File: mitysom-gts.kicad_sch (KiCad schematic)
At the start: 9 parts, among them J1 Plug_Samtec_SEAM-50-02.0-L-08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

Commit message: [#100764] Swap DC-SCM PCIe P/N for better PCB layout
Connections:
- net DC_SCM_PCIE.TX0+: now also J1.G38 (GTSL1B_RX_CH0_N); no longer J1.G39 (GTSL1B_RX_CH0_P)
- net DC_SCM_PCIE.TX0-: now also J1.G39 (GTSL1B_RX_CH0_P); no longer J1.G38 (GTSL1B_RX_CH0_N)
- net DC_SCM_PCIE.TX1+: now also J1.A36 (GTSL1B_RX_CH1_N); no longer J1.A37 (GTSL1B_RX_CH1_P)
- net DC_SCM_PCIE.TX1-: now also J1.A37 (GTSL1B_RX_CH1_P); no longer J1.A36 (GTSL1B_RX_CH1_N)
- net DC_SCM_PCIE.TX2+: now also J1.G42 (GTSL1B_RX_CH2_N); no longer J1.G43 (GTSL1B_RX_CH2_P)
- net DC_SCM_PCIE.TX2-: now also J1.G43 (GTSL1B_RX_CH2_P); no longer J1.G42 (GTSL1B_RX_CH2_N)
- net DC_SCM_PCIE.TX3+: now also J1.A40 (GTSL1B_RX_CH3_N); no longer J1.A41 (GTSL1B_RX_CH3_P)
- net DC_SCM_PCIE.TX3-: now also J1.A41 (GTSL1B_RX_CH3_P); no longer J1.A40 (GTSL1B_RX_CH3_N)
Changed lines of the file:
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@@
 		)
 	)
-	(label "DC_SCM_PCIE.TX1+"
-		(at 133.4377 187.96 0)
+	(label "DC_SCM_PCIE.TX3+"
+		(at 133.35 200.66 0)
 		(effects
 			(font
@@
 		)
 	)
-	(label "DC_SCM_PCIE.TX3+"
-		(at 133.4377 198.12 0)
+	(label "DC_SCM_PCIE.TX1-"
+		(at 133.35 187.96 0)
 		(effects
 			(font
@@
 		)
 	)
-	(label "DC_SCM_PCIE.TX2-"
-		(at 133.35 195.58 0)
+	(label "DC_SCM_PCIE.TX3-"
+		(at 133.35 198.12 0)
 		(effects
 			(font
@@
 		)
 	)
-	(label "DC_SCM_PCIE.TX3-"
-		(at 133.4377 200.66 0)
+	(label "DC_SCM_PCIE.TX2-"
+		(at 133.35 193.04 0)
 		(effects
 			(font
@@
 		)
 	)
+	(label "DC_SCM_PCIE.TX0-"
+		(at 133.35 182.88 0)
+		(effects
+			(font
+				(size 1.27 1.27)
+			)
+			(justify left bottom)
+		)
+	)
 	(label "DP.TXD0-"
 		(at 280.67 119.38 0)
@@
 		)
 	)
+	(label "DC_SCM_PCIE.TX0+"
+		(at 133.35 185.42 0)
+		(effects
+			(font
+				(size 1.27 1.27)
+			)
+			(justify left bottom)
+		)
+	)
 	(label "ROOTPORT.TX0-"
 		(at 135.89 130.81 0)
@@
 		)
 	)
-	(label "DC_SCM_PCIE.TX0-"
-		(at 133.4377 185.42 0)
-		(effects
-			(font
-				(size 1.27 1.27)
-			)
-			(justify left bottom)
-		)
-	)
 	(label "PCIEx4_CLK.CLK+"
 		(at 134.62 204.47 0)
@@
 		)
 	)
-	(label "DC_SCM_PCIE.TX1-"
-		(at 133.4377 190.5 0)
-		(effects
-			(font
-				(size 1.27 1.27)
-			)
-			(justify left bottom)
-		)
-	)
 	(label "156_25MHz_CLK.+"
 		(at 133.35 154.94 0)
@@
 		)
 	)
+	(label "DC_SCM_PCIE.TX2+"
+		(at 133.35 195.58 0)
+		(effects
+			(font
+				(size 1.27 1.27)
+			)
+			(justify left bottom)
+		)
+	)
 	(label "DC_SCM_PCIE.RX2+"
 		(at 133.4377 171.45 0)
@@
 		)
 	)
-	(label "DC_SCM_PCIE.TX0+"
-		(at 133.4377 182.88 0)
+	(label "DC_SCM_PCIE.TX1+"
+		(at 133.35 190.5 0)
 		(effects
 			(font
@@
 		(effects
 			(font
-				(size 1.27 1.27)
-			)
-			(justify left bottom)
-		)
-	)
-	(label "DC_SCM_PCIE.TX2+"
-		(at 133.35 193.04 0)
-		(effects
-			(font

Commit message: [#100707] Place PCIe AC coupling capacitors
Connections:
- net DC_SCM_PCIE.RX1+: now also J1.H40 (GTSL1B_TX_CH1_N); no longer J1.H41 (GTSL1B_TX_CH1_P)
- net DC_SCM_PCIE.RX1-: now also J1.H41 (GTSL1B_TX_CH1_P); no longer J1.H40 (GTSL1B_TX_CH1_N)
- net DC_SCM_PCIE.RX3+: now also J1.H48 (GTSL1B_TX_CH3_N); no longer J1.H49 (GTSL1B_TX_CH3_P)
- net DC_SCM_PCIE.RX3-: now also J1.H49 (GTSL1B_TX_CH3_P); no longer J1.H48 (GTSL1B_TX_CH3_N)
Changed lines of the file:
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@@
 		)
 	)
-	(label "DC_SCM_PCIE.RX3+"
+	(label "DC_SCM_PCIE.RX3-"
 		(at 133.4377 176.53 0)
 		(effects
@@
 		)
 	)
-	(label "DC_SCM_PCIE.RX3-"
+	(label "DC_SCM_PCIE.RX3+"
 		(at 133.4377 179.07 0)
 		(effects
@@
 		)
 	)
-	(label "DC_SCM_PCIE.RX1-"
+	(label "DC_SCM_PCIE.RX1+"
 		(at 133.4076 168.91 0)
 		(effects
@@
 		)
 	)
-	(label "DC_SCM_PCIE.RX1+"
+	(label "DC_SCM_PCIE.RX1-"
 		(at 133.4076 166.37 0)
 		(effects

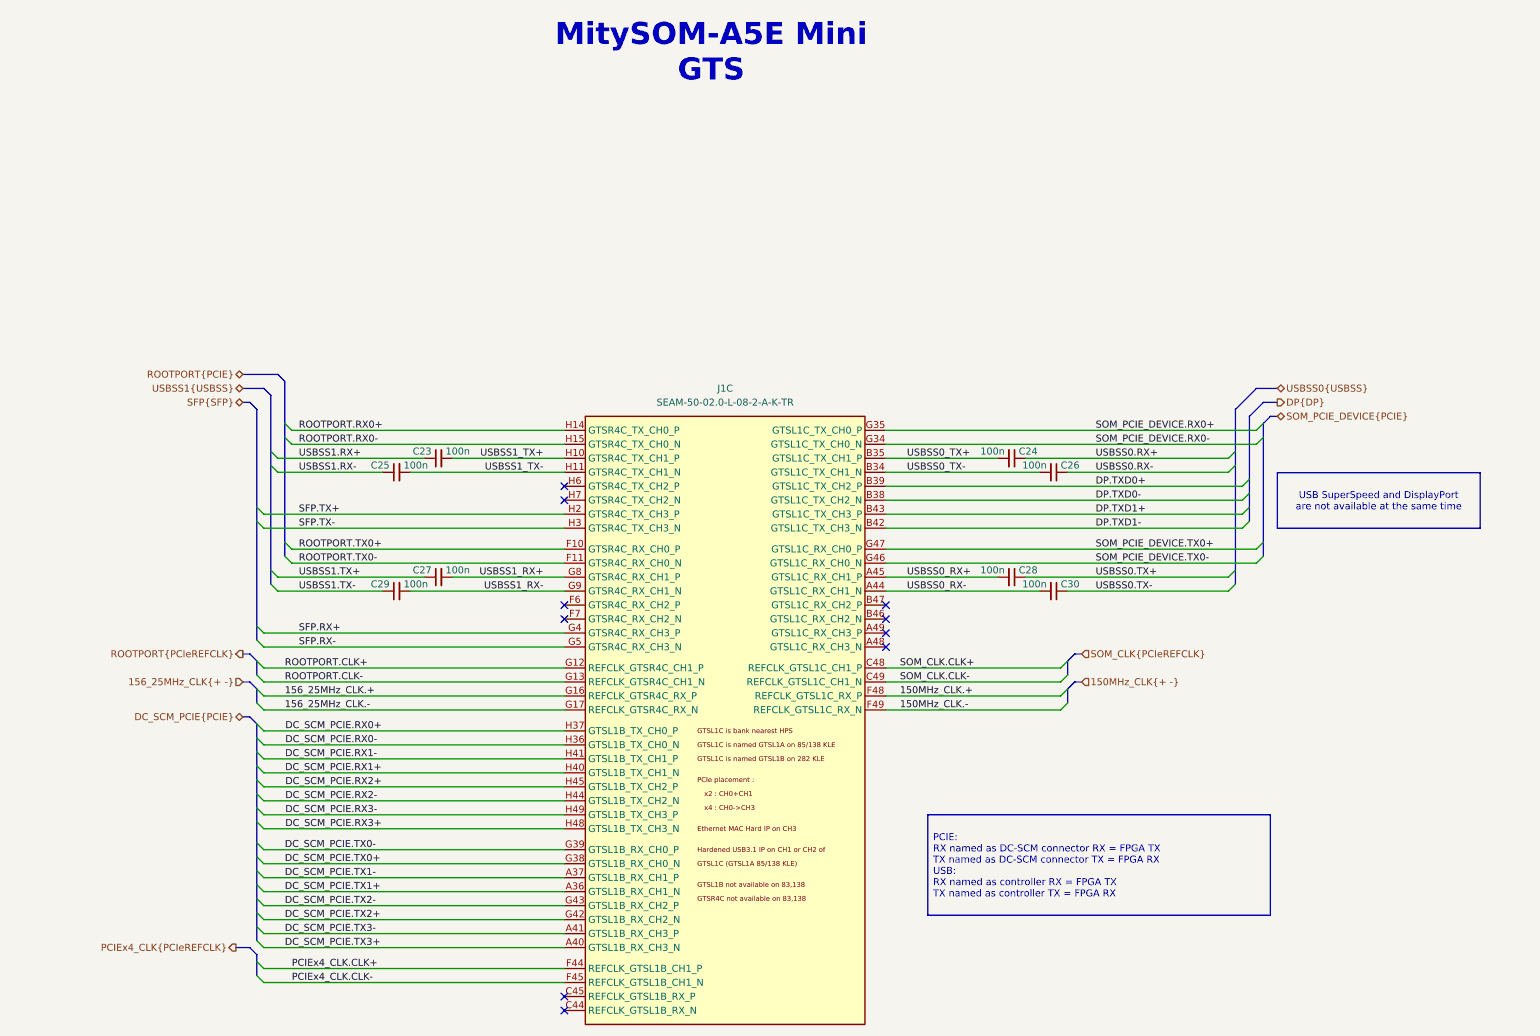
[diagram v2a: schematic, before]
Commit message: [#100707] Move PCIe AC coupling capacitrs on the schematic, close to TX source, add 0Rs to DC-SCM PCIe
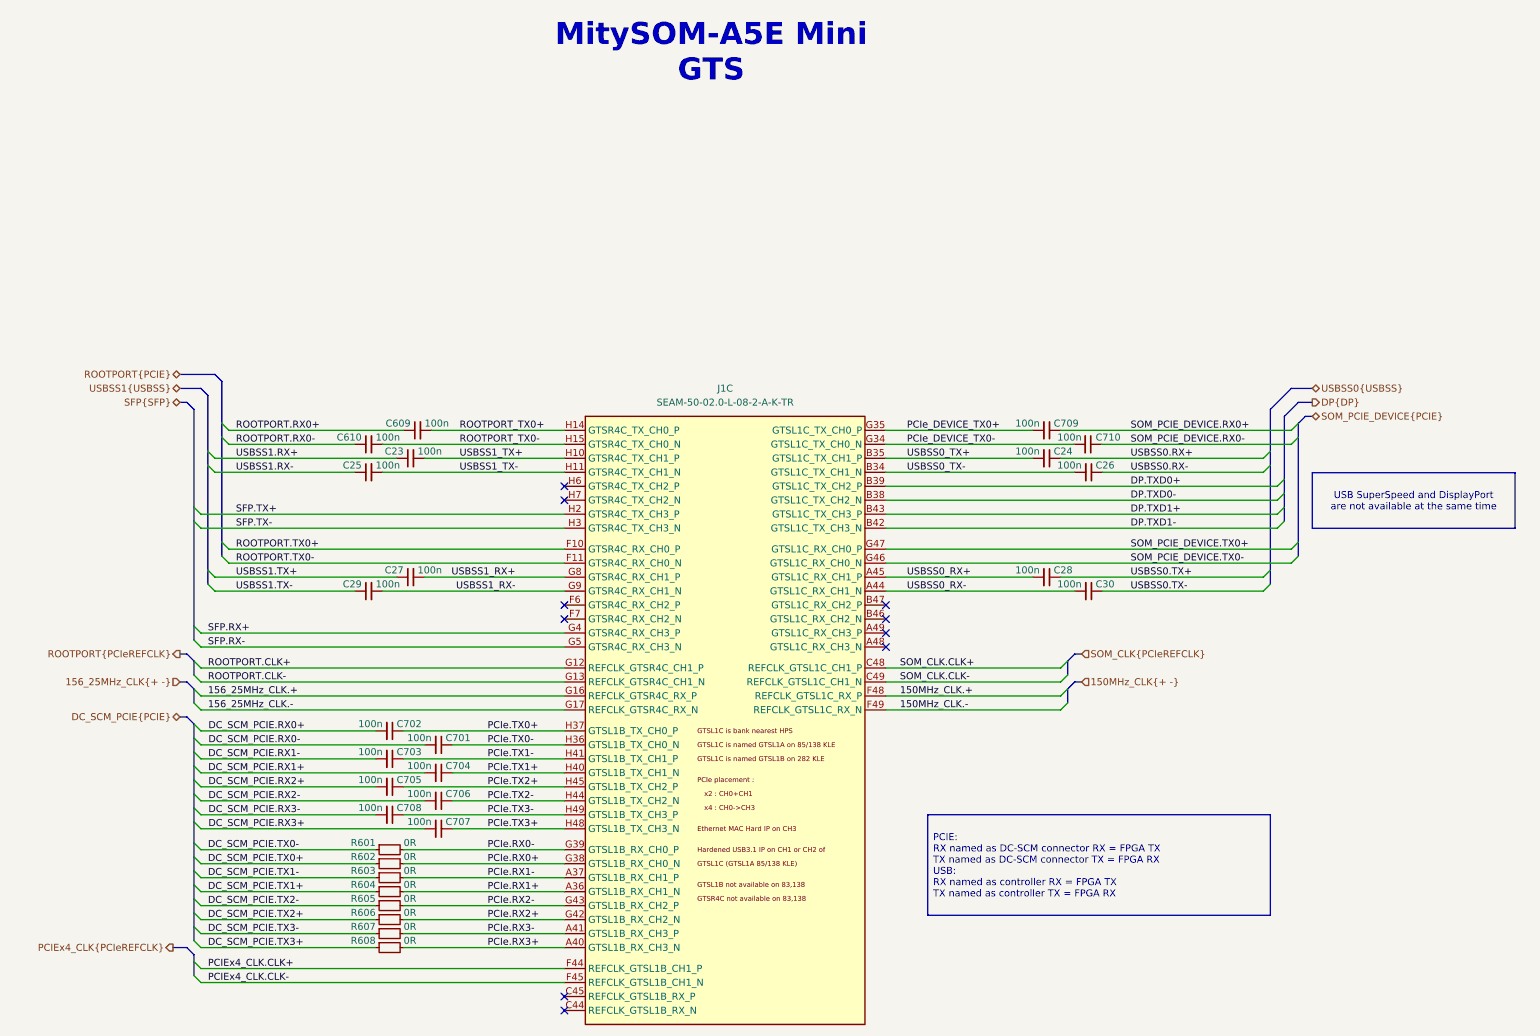
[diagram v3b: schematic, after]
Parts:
- added C609, C610, C701, C702, C703, C704, C705, C706, C707, C708, C709, C710: C_100n_0402, antmicro-footprints:C_0402_1005Metric, symbol antmicroCapacitors0402:C_100n_0402
- added R601, R602, R603, R604, R605, R606, R607, R608: R_0R_0402, antmicro-footprints:R_0402_1005Metric, symbol antmicroResistors0402:R_0R_0402
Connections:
- net DC_SCM_PCIE.RX0+: now also C702.2; no longer J1.H37 (GTSL1B_TX_CH0_P)
- net DC_SCM_PCIE.RX0-: now also C701.2; no longer J1.H36 (GTSL1B_TX_CH0_N)
- net DC_SCM_PCIE.RX1+: now also C704.2; no longer J1.H40 (GTSL1B_TX_CH1_N)
- net DC_SCM_PCIE.RX1-: now also C703.2; no longer J1.H41 (GTSL1B_TX_CH1_P)
- net DC_SCM_PCIE.RX2+: now also C705.2; no longer J1.H45 (GTSL1B_TX_CH2_P)
- net DC_SCM_PCIE.RX2-: now also C706.2; no longer J1.H44 (GTSL1B_TX_CH2_N)
- net DC_SCM_PCIE.RX3+: now also C707.2; no longer J1.H48 (GTSL1B_TX_CH3_N)
- net DC_SCM_PCIE.RX3-: now also C708.2; no longer J1.H49 (GTSL1B_TX_CH3_P)
- net DC_SCM_PCIE.TX0+: now also R602.1; no longer J1.G38 (GTSL1B_RX_CH0_N)
- net DC_SCM_PCIE.TX0-: now also R601.1; no longer J1.G39 (GTSL1B_RX_CH0_P)
- net DC_SCM_PCIE.TX1+: now also R604.1; no longer J1.A36 (GTSL1B_RX_CH1_N)
- net DC_SCM_PCIE.TX1-: now also R603.1; no longer J1.A37 (GTSL1B_RX_CH1_P)
- net DC_SCM_PCIE.TX2+: now also R606.1; no longer J1.G42 (GTSL1B_RX_CH2_N)
- net DC_SCM_PCIE.TX2-: now also R605.1; no longer J1.G43 (GTSL1B_RX_CH2_P)
- net DC_SCM_PCIE.TX3+: now also R608.1; no longer J1.A40 (GTSL1B_RX_CH3_N)
- net DC_SCM_PCIE.TX3-: now also R607.1; no longer J1.A41 (GTSL1B_RX_CH3_P)
- net ROOTPORT.RX0+: now also C609.1; no longer J1.H14 (GTSR4C_TX_CH0_P)
- net ROOTPORT.RX0-: now also C610.1; no longer J1.H15 (GTSR4C_TX_CH0_N)
- net SOM_PCIE_DEVICE.RX0+: now also C709.1; no longer J1.G35 (GTSL1C_TX_CH0_P)
- net SOM_PCIE_DEVICE.RX0-: now also C710.1; no longer J1.G34 (GTSL1C_TX_CH0_N)
- new net PCIe.RX0+: J1.G38 (GTSL1B_RX_CH0_N), R602.2
- new net PCIe.RX0-: J1.G39 (GTSL1B_RX_CH0_P), R601.2
- new net PCIe.RX1+: J1.A36 (GTSL1B_RX_CH1_N), R604.2
- new net PCIe.RX1-: J1.A37 (GTSL1B_RX_CH1_P), R603.2
- new net PCIe.RX2+: J1.G42 (GTSL1B_RX_CH2_N), R606.2
- new net PCIe.RX2-: J1.G43 (GTSL1B_RX_CH2_P), R605.2
- new net PCIe.RX3+: J1.A40 (GTSL1B_RX_CH3_N), R608.2
- new net PCIe.RX3-: J1.A41 (GTSL1B_RX_CH3_P), R607.2
- new net PCIe.TX0+: C702.1, J1.H37 (GTSL1B_TX_CH0_P)
- new net PCIe.TX0-: C701.1, J1.H36 (GTSL1B_TX_CH0_N)
- new net PCIe.TX1+: C704.1, J1.H40 (GTSL1B_TX_CH1_N)
- new net PCIe.TX1-: C703.1, J1.H41 (GTSL1B_TX_CH1_P)
- new net PCIe.TX2+: C705.1, J1.H45 (GTSL1B_TX_CH2_P)
- new net PCIe.TX2-: C706.1, J1.H44 (GTSL1B_TX_CH2_N)
- new net PCIe.TX3+: C707.1, J1.H48 (GTSL1B_TX_CH3_N)
- new net PCIe.TX3-: C708.1, J1.H49 (GTSL1B_TX_CH3_P)
- new net PCIe_DEVICE_TX0+: C709.2, J1.G35 (GTSL1C_TX_CH0_P)
- new net PCIe_DEVICE_TX0-: C710.2, J1.G34 (GTSL1C_TX_CH0_N)
- new net ROOTPORT_TX0+: C609.2, J1.H14 (GTSR4C_TX_CH0_P)
- new net ROOTPORT_TX0-: C610.2, J1.H15 (GTSR4C_TX_CH0_N)
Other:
- moved on the sheet: C23, C24, C25, C26, C27, C28, C29, C30

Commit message: [#101340] Add flash sockets
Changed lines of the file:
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@@
 	(wire
 		(pts
-			(xy 281.8161 109.22) (xy 316.23 109.22)
+			(xy 281.94 109.22) (xy 316.23 109.22)
 		)
 		(stroke
@@
 	(wire
 		(pts
-			(xy 242.57 109.22) (xy 276.7361 109.22)
+			(xy 242.57 109.22) (xy 276.86 109.22)
 		)
 		(stroke
@@
 	(symbol
 		(lib_id "antmicroCapacitors0402:C_100n_0402")
-		(at 281.8161 109.22 0)
+		(at 281.94 109.22 0)
 		(mirror y)
 		(unit 1)
@@
 		(dnp no)
 		(property "Reference" "C710"
-			(at 280.67 107.95 0)
+			(at 280.7939 107.95 0)
 			(show_name no)
 			(do_not_autoplace no)
@@
 		)
 		(property "Value" "C_100n_0402"
-			(at 261.4961 119.38 0)
+			(at 261.62 119.38 0)
 			(hide yes)
 			(show_name no)
@@
 		)
 		(property "Footprint" "antmicro-footprints:C_0402_1005Metric"
-			(at 261.4961 121.92 0)
+			(at 261.62 121.92 0)
 			(hide yes)
 			(show_name no)
@@
 		)
 		(property "Datasheet" "https://www.murata.com/products/productdetail?partno=GRM155R61H104KE14%23"
-			(at 261.4961 124.46 0)
+			(at 261.62 124.46 0)
 			(hide yes)
 			(show_name no)
@@
 		)
 		(property "Description" "SMD Multilayer Ceramic Capacitor, 0.1 µF, 50 V, 0402 [1005 Metric], ± 10%, X5R, GRM Series"
-			(at 281.8161 109.22 0)
+			(at 281.94 109.22 0)
 			(hide yes)
 			(show_name no)
@@
 		)
 		(property "MPN" "GRM155R61H104KE14D"
-			(at 261.4961 127 0)
+			(at 261.62 127 0)
 			(hide yes)
 			(show_name no)
@@
 		)
 		(property "Manufacturer" "Murata"
-			(at 261.4961 129.54 0)
+			(at 261.62 129.54 0)
 			(hide yes)
 			(show_name no)
@@
 		)
 		(property "License" "Apache-2.0"
-			(at 261.4961 132.08 0)
+			(at 261.62 132.08 0)
 			(hide yes)
 			(show_name no)
@@
 		)
 		(property "Author" "Antmicro"
-			(at 261.4961 134.62 0)
+			(at 261.62 134.62 0)
 			(hide yes)
 			(show_name no)
@@
 		)
 		(property "Val" "100n"
-			(at 278.13 107.95 0)
+			(at 278.2539 107.95 0)
 			(show_name no)
 			(do_not_autoplace no)
@@
 		)
 		(property "Voltage" "50V"
-			(at 261.4961 137.16 0)
+			(at 261.62 137.16 0)
 			(hide yes)
 			(show_name no)
@@
 		)
 		(property "Dielectric" "X5R"
-			(at 261.4961 139.7 0)
+			(at 261.62 139.7 0)
 			(hide yes)
 			(show_name no)
